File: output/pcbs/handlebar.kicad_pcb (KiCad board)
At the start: 2 copper layers, 153.6 x 106.8 mm, 59 parts

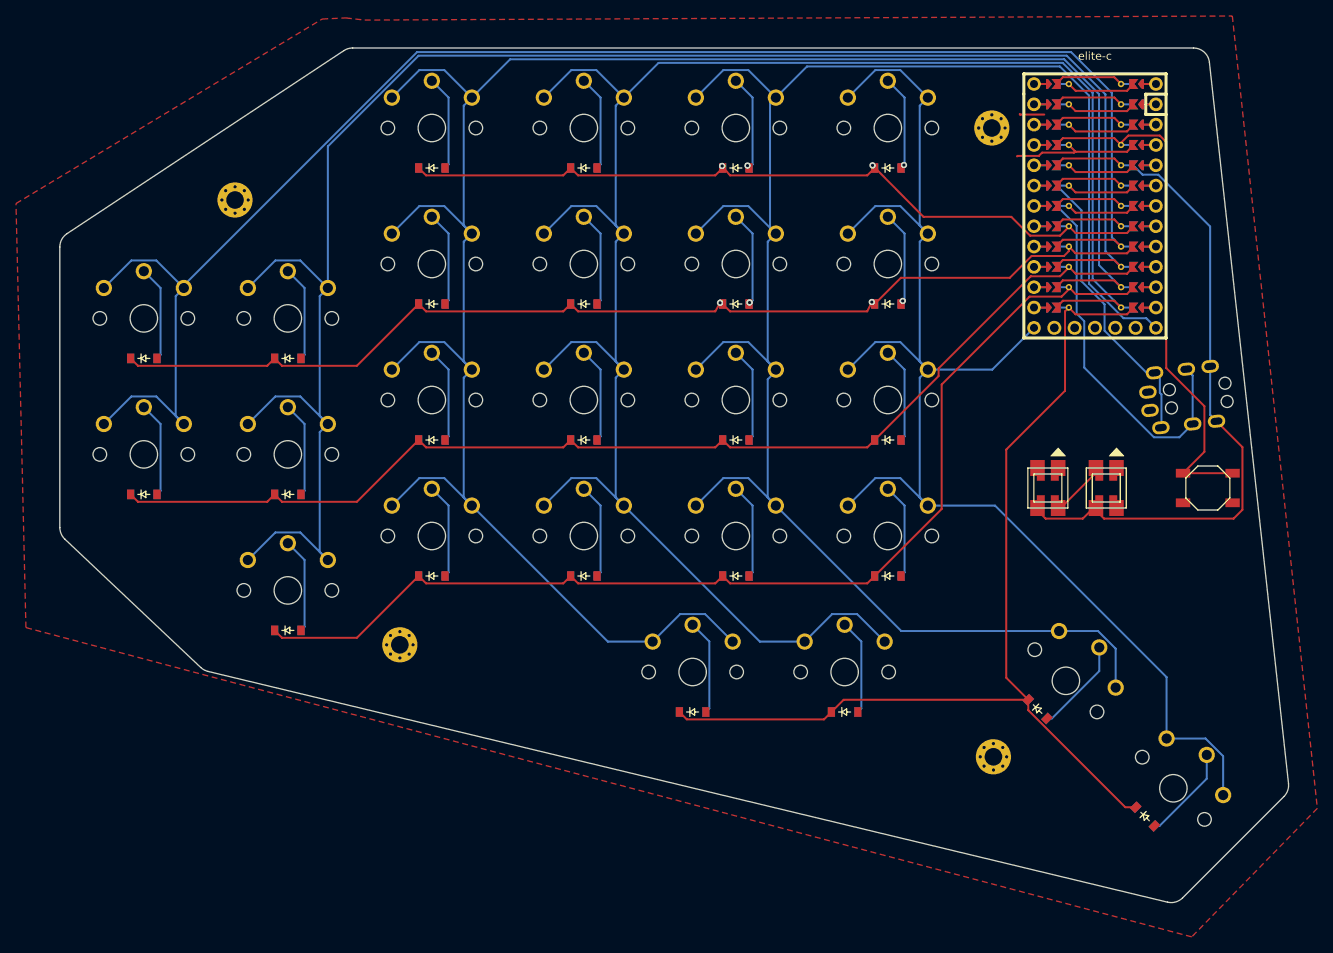
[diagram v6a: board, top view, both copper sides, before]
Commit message: Added vias to the diodes. Changed holes for the MCU. Made space for the resistors. Inverted the switches pins to diodes. Rotated the indicators.
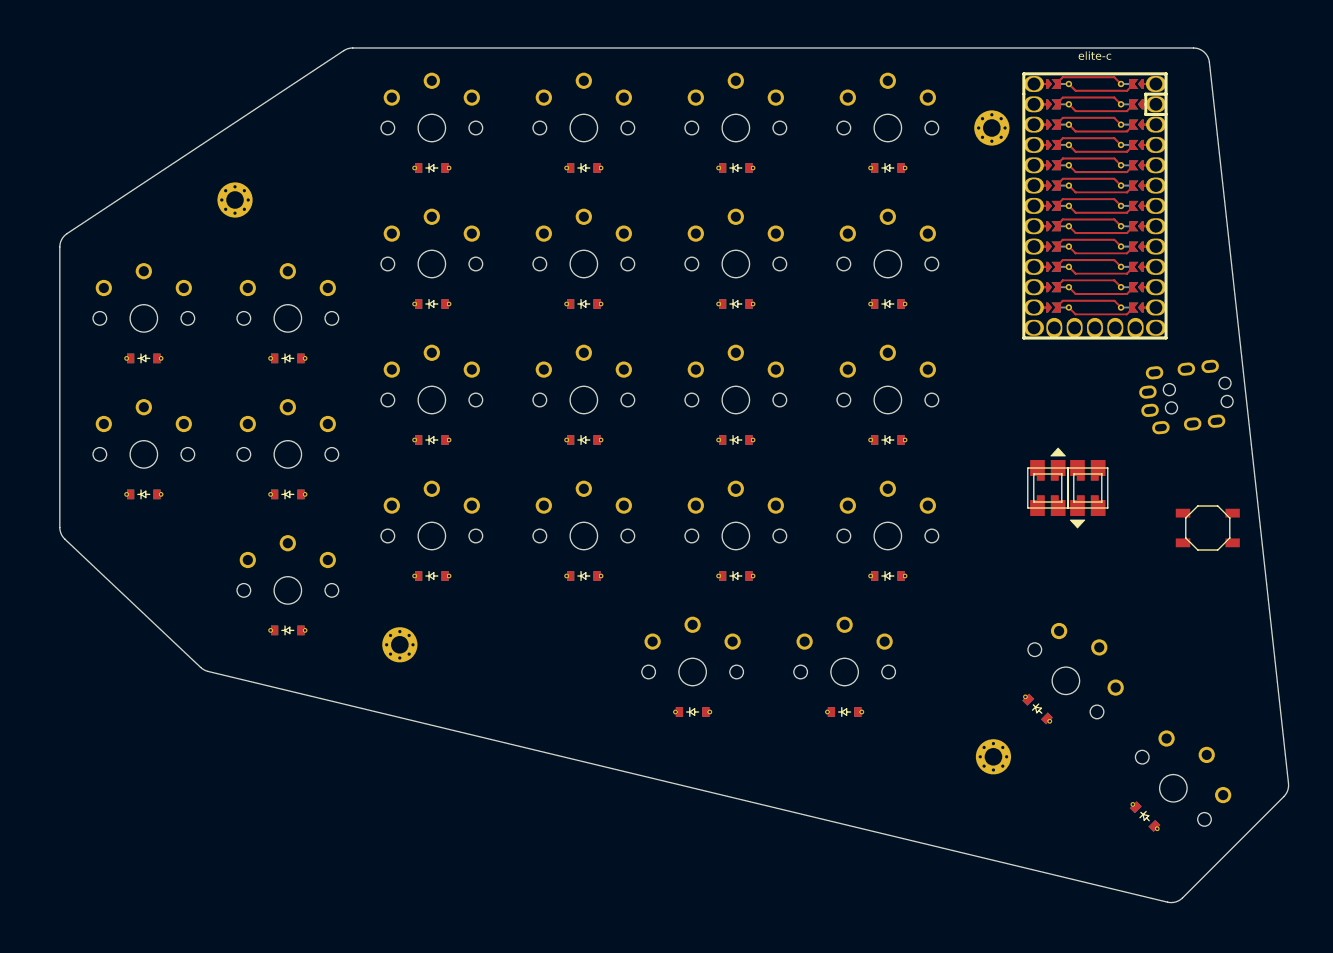
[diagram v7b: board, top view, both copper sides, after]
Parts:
- removed _2, _3, _4, _5: , MountingHole_2.2mm_M2_Pad_Via
- added REF**: VIA-0.6mm, VIA-0.6mm, F.Cu at (97.8, 105.0)
- added REF**: VIA-0.6mm, VIA-0.6mm, F.Cu at (135.8, 88.0)
- added REF**: VIA-0.6mm, VIA-0.6mm, F.Cu at (135.8, 71.0)
- added REF**: VIA-0.6mm, VIA-0.6mm, F.Cu at (135.8, 54.0)
- added REF**: VIA-0.6mm, VIA-0.6mm, F.Cu at (154.8, 105.0)
- added REF**: VIA-0.6mm, VIA-0.6mm, F.Cu at (154.8, 88.0)
- added REF**: VIA-0.6mm, VIA-0.6mm, F.Cu at (154.8, 71.0)
- added REF**: VIA-0.6mm, VIA-0.6mm, F.Cu at (154.8, 54.0)
- added REF**: VIA-0.6mm, VIA-0.6mm, F.Cu at (61.9, 94.8)
- added REF**: VIA-0.6mm, VIA-0.6mm, F.Cu at (61.9, 77.8)
- added REF**: VIA-0.6mm, VIA-0.6mm, F.Cu at (79.8, 111.8)
- added REF**: VIA-0.6mm, VIA-0.6mm, F.Cu at (97.8, 88.0)
- added REF**: VIA-0.6mm, VIA-0.6mm, F.Cu at (79.8, 94.8)
- added REF**: VIA-0.6mm, VIA-0.6mm, F.Cu at (79.8, 77.8)
- added REF**: VIA-0.6mm, VIA-0.6mm, F.Cu at (130.4, 122.0)
- added REF**: VIA-0.6mm, VIA-0.6mm, F.Cu at (149.4, 122.0)
- added REF**: VIA-0.6mm, VIA-0.6mm, F.Cu at (174.2, 120.1)
- added REF**: VIA-0.6mm, VIA-0.6mm, F.Cu at (187.6, 133.6)
- added REF**: VIA-0.6mm, VIA-0.6mm, F.Cu at (102.2, 105.0)
- added REF**: VIA-0.6mm, VIA-0.6mm, F.Cu at (102.2, 88.0)
- added REF**: VIA-0.6mm, VIA-0.6mm, F.Cu at (102.2, 71.0)
- added REF**: VIA-0.6mm, VIA-0.6mm, F.Cu at (102.2, 54.0)
- added REF**: VIA-0.6mm, VIA-0.6mm, F.Cu at (97.8, 71.0)
- added REF**: VIA-0.6mm, VIA-0.6mm, F.Cu at (121.2, 105.0)
- added REF**: VIA-0.6mm, VIA-0.6mm, F.Cu at (121.2, 88.0)
- added REF**: VIA-0.6mm, VIA-0.6mm, F.Cu at (121.2, 71.0)
- added REF**: VIA-0.6mm, VIA-0.6mm, F.Cu at (121.2, 54.0)
- added REF**: VIA-0.6mm, VIA-0.6mm, F.Cu at (140.2, 105.0)
- added REF**: VIA-0.6mm, VIA-0.6mm, F.Cu at (140.2, 88.0)
- added REF**: VIA-0.6mm, VIA-0.6mm, F.Cu at (140.2, 71.0)
- added REF**: VIA-0.6mm, VIA-0.6mm, F.Cu at (140.2, 54.0)
- added REF**: VIA-0.6mm, VIA-0.6mm, F.Cu at (159.2, 105.0)
- added REF**: VIA-0.6mm, VIA-0.6mm, F.Cu at (159.2, 88.0)
- added REF**: VIA-0.6mm, VIA-0.6mm, F.Cu at (97.8, 54.0)
- added REF**: VIA-0.6mm, VIA-0.6mm, F.Cu at (159.2, 71.0)
- added REF**: VIA-0.6mm, VIA-0.6mm, F.Cu at (159.2, 54.0)
- added REF**: VIA-0.6mm, VIA-0.6mm, F.Cu at (66.2, 94.8)
- added REF**: VIA-0.6mm, VIA-0.6mm, F.Cu at (66.2, 77.8)
- added REF**: VIA-0.6mm, VIA-0.6mm, F.Cu at (84.2, 111.8)
- added REF**: VIA-0.6mm, VIA-0.6mm, F.Cu at (84.2, 94.8)
- added REF**: VIA-0.6mm, VIA-0.6mm, F.Cu at (84.2, 77.8)
- added REF**: VIA-0.6mm, VIA-0.6mm, F.Cu at (134.8, 122.0)
- added REF**: VIA-0.6mm, VIA-0.6mm, F.Cu at (153.8, 122.0)
- added REF**: VIA-0.6mm, VIA-0.6mm, F.Cu at (177.2, 123.2)
- added REF**: VIA-0.6mm, VIA-0.6mm, F.Cu at (116.8, 105.0)
- added REF**: VIA-0.6mm, VIA-0.6mm, F.Cu at (190.7, 136.6)
- added REF**: VIA-0.6mm, VIA-0.6mm, F.Cu at (116.8, 88.0)
- added REF**: VIA-0.6mm, VIA-0.6mm, F.Cu at (116.8, 71.0)
- added REF**: VIA-0.6mm, VIA-0.6mm, F.Cu at (116.8, 54.0)
- added REF**: VIA-0.6mm, VIA-0.6mm, F.Cu at (135.8, 105.0)
- added _52: , MountingHole_2.2mm_M2_Pad_Via, F.Cu at (75.4, 58.0)
- added _53: , MountingHole_2.2mm_M2_Pad_Via, F.Cu at (96.0, 113.6)
- added _54: , MountingHole_2.2mm_M2_Pad_Via, F.Cu at (170.0, 49.0)
- added _55: , MountingHole_2.2mm_M2_Pad_Via, F.Cu at (170.2, 127.6)
- moved rst1 5.00 mm to (197.0, 99.0)
- moved I2 2.30 mm to (182.0, 94.0), turned to -90 degrees
- renumbered B1 to rst1
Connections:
- net _1_14 renamed _51_14
- net _1_15 renamed _51_15
- net _1_16 renamed _51_16
- net _1_17 renamed _51_17
- net _1_18 renamed _51_18
- net _1_19 renamed _51_19
- net _1_20 renamed _51_20
- net _1_21 renamed _51_21
- net _1_22 renamed _51_22
- net _1_23 renamed _51_23
- net _1_24 renamed _51_24
- ? pad 25: VBUS -> _51_25
- S1 pad 1: n_ring -> ring_bottom
- S1 pad 2: ring_bottom -> n_ring
- S10 pad 1: n_index -> index_home
- S10 pad 2: index_home -> n_index
- S11 pad 1: n_index -> index_top
- S11 pad 2: index_top -> n_index
- S12 pad 1: n_index -> index_nums
- S12 pad 2: index_nums -> n_index
- S13 pad 1: n_inner -> inner_bottom
- S13 pad 2: inner_bottom -> n_inner
- S14 pad 1: n_inner -> inner_home
- S14 pad 2: inner_home -> n_inner
- S15 pad 1: n_inner -> inner_top
- S15 pad 2: inner_top -> n_inner
- S16 pad 1: n_inner -> inner_nums
- S16 pad 2: inner_nums -> n_inner
- S17 pad 1: n_outer -> outer_home
- S17 pad 2: outer_home -> n_outer
- S18 pad 1: n_outer -> outer_top
- S18 pad 2: outer_top -> n_outer
- S19 pad 1: n_pinky -> pinky_bottom
- S19 pad 2: pinky_bottom -> n_pinky
- S2 pad 1: n_ring -> ring_home
- S2 pad 2: ring_home -> n_ring
- S20 pad 1: n_pinky -> pinky_home
- S20 pad 2: pinky_home -> n_pinky
- S21 pad 1: n_pinky -> pinky_top
- S21 pad 2: pinky_top -> n_pinky
- S22 pad 1: n_ring -> left_thumb
- S22 pad 2: left_thumb -> n_ring
- S23 pad 1: n_middle -> right_thumb
- S23 pad 2: right_thumb -> n_middle
- S24 pad 1: n_index -> center_thumb
- S24 pad 2: center_thumb -> n_index
- S25 pad 1: n_inner -> inner_thumb
- S25 pad 2: inner_thumb -> n_inner
- S3 pad 1: n_ring -> ring_top
- S3 pad 2: ring_top -> n_ring
- S4 pad 1: n_ring -> ring_nums
- S4 pad 2: ring_nums -> n_ring
- S5 pad 1: n_middle -> middle_bottom
- S5 pad 2: middle_bottom -> n_middle
- S6 pad 1: n_middle -> middle_home
- S6 pad 2: middle_home -> n_middle
- S7 pad 1: n_middle -> middle_top
- S7 pad 2: middle_top -> n_middle
- S8 pad 1: n_middle -> middle_nums
- S8 pad 2: middle_nums -> n_middle
- S9 pad 1: n_index -> index_bottom
- S9 pad 2: index_bottom -> n_index
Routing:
- net (no net): track 11.1 -> 342.9 mm
- net n_ring: track 265.2 -> 0.00 mm
- net n_middle: track 248.0 -> 0.00 mm
- net n_index: track 235.9 -> 0.00 mm
- net n_pinky: track 228.5 -> 0.00 mm
- net n_outer: track 204.0 -> 0.00 mm
- net n_inner: track 179.6 -> 0.00 mm
- net n_home: track 143.8 -> 0.00 mm
- net n_bottom: track 139.7 -> 0.00 mm
- net n_top: track 138.2 -> 0.00 mm, vias 2 -> 0
- net n_thumb: track 128.5 -> 0.00 mm
- net n_nums: track 99.2 -> 0.00 mm, vias 2 -> 0
- net n_vcc: track 88.2 -> 0.00 mm
- net n_reset: track 67.6 -> 0.00 mm
- net n_scl: track 57.0 -> 0.00 mm
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- removed copper zone on F.Cu, net n_gnd
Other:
- net class Default added: clearance 0.2, trace_width 0.25, via_dia 0.8, via_drill 0.4

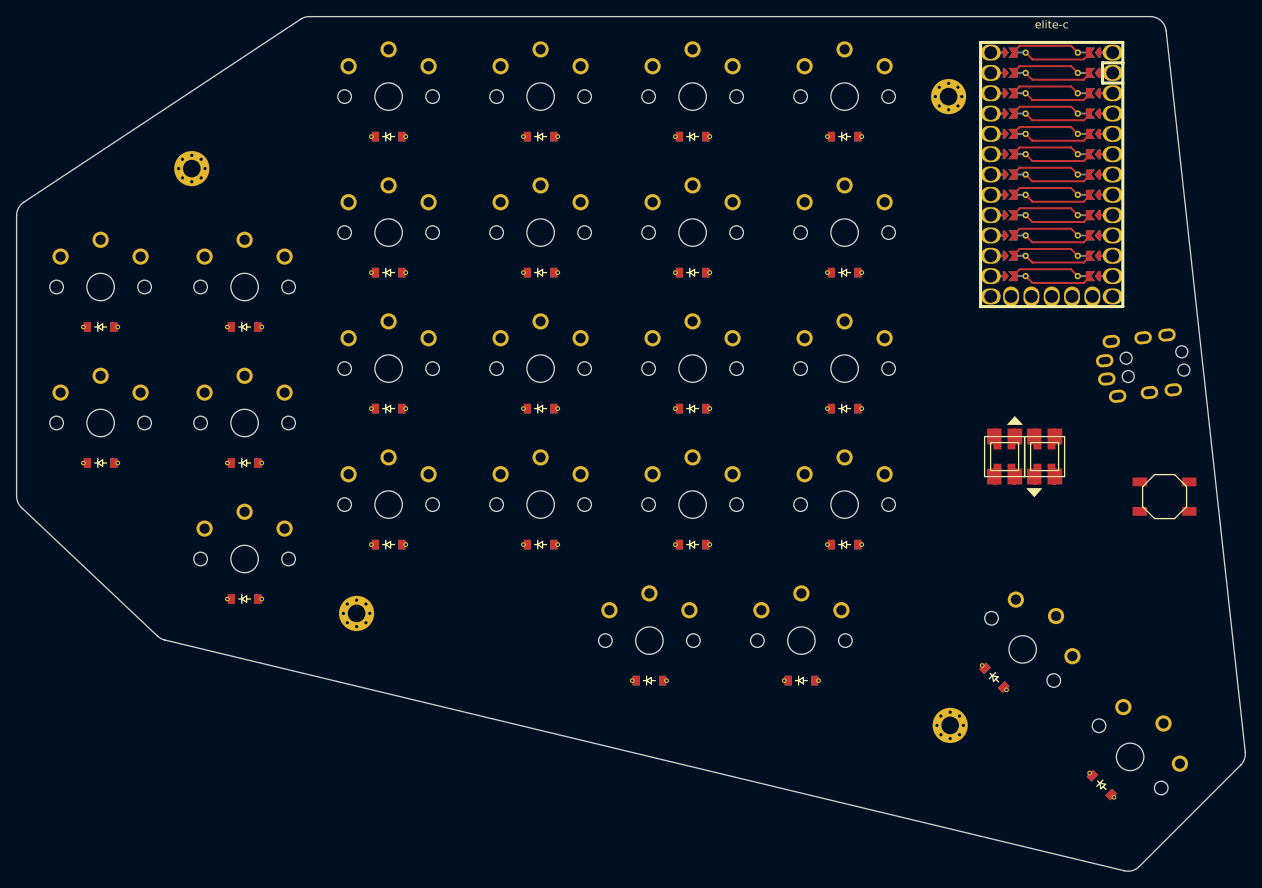
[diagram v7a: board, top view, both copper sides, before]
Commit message: Removed/replaced the "outer" column. Reoriented the indicators. Rearranged the pin assignments. More instructions post-Ergogen.
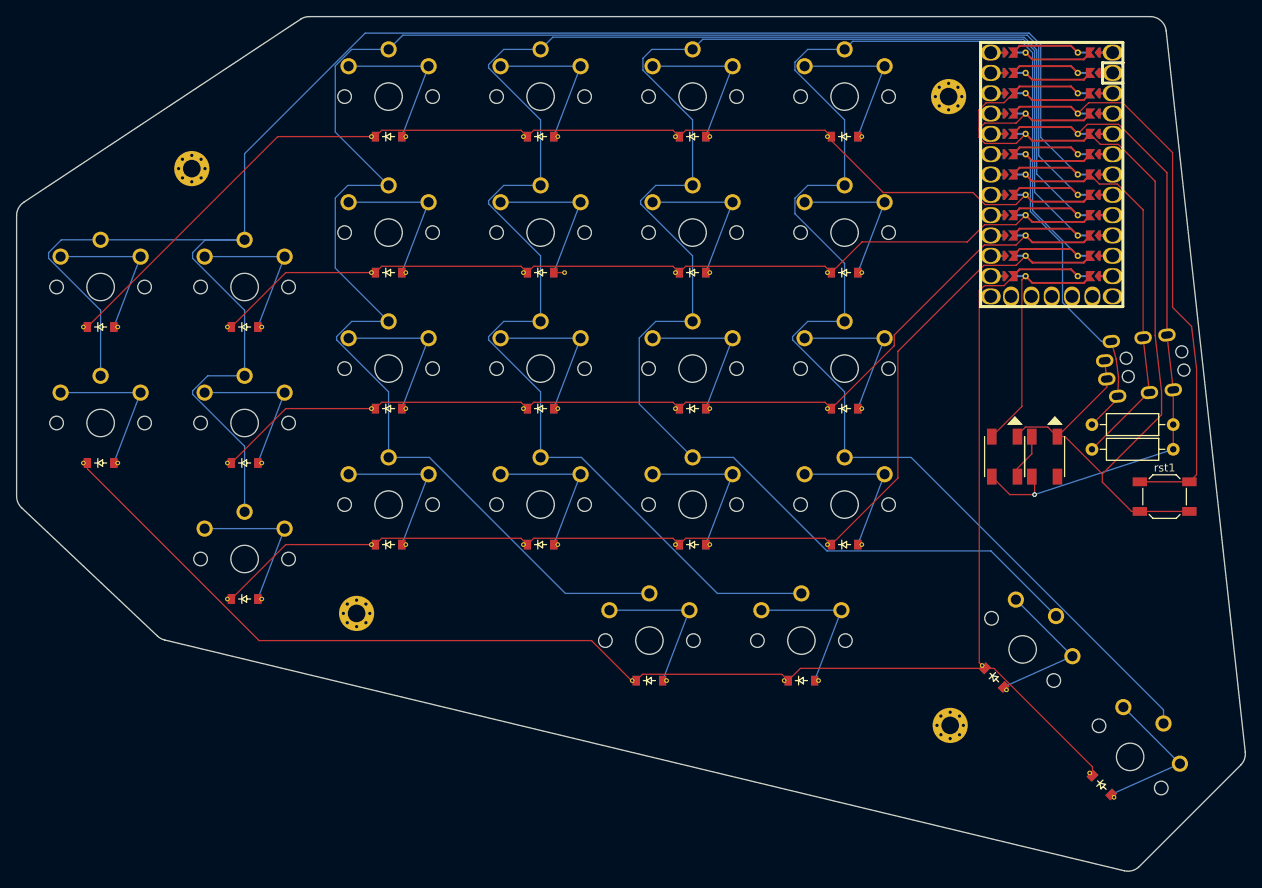
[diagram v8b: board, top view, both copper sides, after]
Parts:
- removed the REF** at (174.2, 120.1)
- removed the REF** at (187.6, 133.6)
- removed the REF** at (121.2, 71.0)
- removed the REF** at (177.2, 123.2)
- removed the REF** at (190.7, 136.6)
- added REF**: VIA-0.6mm, VIA-0.6mm, F.Cu at (122.0, 71.0)
- added REF**: R_Axial_DIN0207_L6.3mm_D2.5mm_P10.16mm_Horizontal, Resistor_THT:R_Axial_DIN0207_L6.3mm_D2.5mm_P10.16mm_Horizontal, F.Cu at (187.9, 90.0)
- added REF**: VIA-0.6mm, VIA-0.6mm, F.Cu at (187.6, 133.6)
- added REF**: VIA-0.6mm, VIA-0.6mm, F.Cu at (174.2, 120.1)
- added REF**: VIA-0.6mm, VIA-0.6mm, F.Cu at (177.2, 123.2)
- added REF**: VIA-0.6mm, VIA-0.6mm, F.Cu at (190.7, 136.6)
- added REF**: R_Axial_DIN0207_L6.3mm_D2.5mm_P10.16mm_Horizontal, Resistor_THT:R_Axial_DIN0207_L6.3mm_D2.5mm_P10.16mm_Horizontal, F.Cu at (187.9, 93.1)
- I1, I2: footprint WS2812B -> Personal:WS2812B
- _52, _53, _54, _55: footprint MountingHole_2.2mm_M2_Pad_Via -> MountingHole:MountingHole_2.2mm_M2_Pad_Via
- rst1: footprint E73:SW_TACT_ALPS_SKQGABE010 -> Button_Switch_SMD:SW_SPST_SKQG_WithoutStem
- turned I2 to 90 degrees
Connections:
- net D2 renamed _51_2
- net D3 renamed _51_1
- net VBUS renamed _51_0
- ? pad 10: n_bottom -> _51_10
- ? pad 11: n_thumb -> _51_11
- ? pad 12: n_inner -> B5
- ? pad 13: n_index -> B6
- ? pad 3: n_gnd -> _51_3
- ? pad 4: n_gnd -> _51_4
- ? pad 5: n_sda -> _51_5
- ? pad 6: n_scl -> _51_6
- ? pad 7: n_nums -> _51_7
- ? pad 8: n_top -> _51_8
- ? pad 9: n_home -> _51_9
- D17 pad 1: n_home -> n_thumb
- D18 pad 1: n_top -> n_nums
- REF** pad 1: n_top -> n_nums
- REF** pad 1: n_home -> n_thumb
- S17 pad 2: n_outer -> n_pinky
- S18 pad 2: n_outer -> n_pinky
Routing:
- net (no net): track 342.9 -> 0.00 mm
- net n_pinky: track 0.00 -> 239.1 mm
- net n_ring: track 0.00 -> 228.9 mm
- net n_middle: track 0.00 -> 211.3 mm
- net n_index: track 0.00 -> 208.6 mm
- net n_thumb: track 0.00 -> 207.7 mm
- net n_inner: track 0.00 -> 191.9 mm
- net n_nums: track 0.00 -> 143.9 mm
- net n_gnd: track 0.00 -> 142.2 mm
- net n_bottom: track 0.00 -> 138.6 mm
- net n_home: track 0.00 -> 124.1 mm
- net n_top: track 0.00 -> 117.3 mm
- net n_vcc: track 0.00 -> 86.0 mm, vias 0 -> 1
- net n_reset: track 0.00 -> 74.0 mm
- net n_scl: track 0.00 -> 51.8 mm
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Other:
- copper layers 2 -> 4
- net class Default removed
- rule pad_to_mask_clearance: 0.05 -> 0
